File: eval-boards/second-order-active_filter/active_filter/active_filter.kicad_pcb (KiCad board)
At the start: 2 copper layers, 66 x 40 mm, 35 parts, among them J1 IN_A, J2 IN_B, J4 OUT_A, J5 OUT_B, U1 ADA4075-2

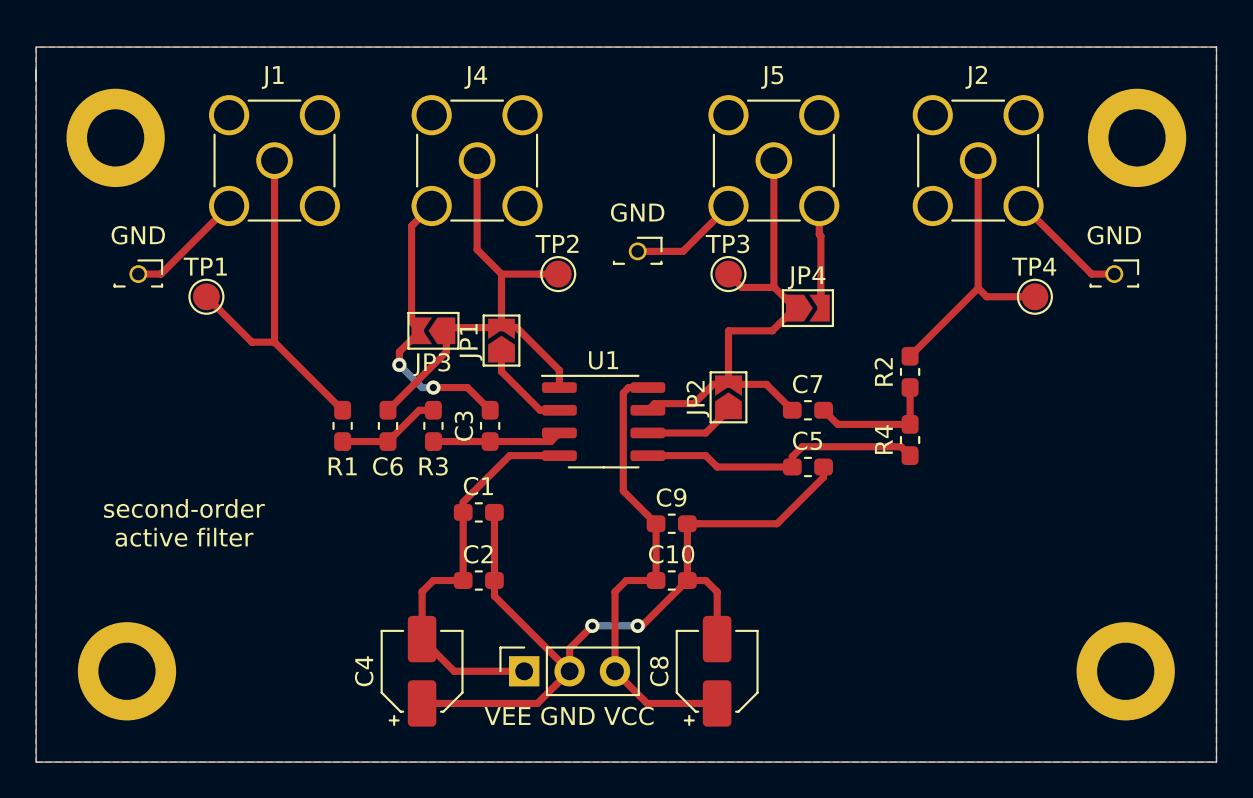
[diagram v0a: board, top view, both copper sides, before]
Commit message: power_and_RF_updated
修正了ADA4817和有源滤波器的电源线管脚、反馈电阻和焊盘handsold
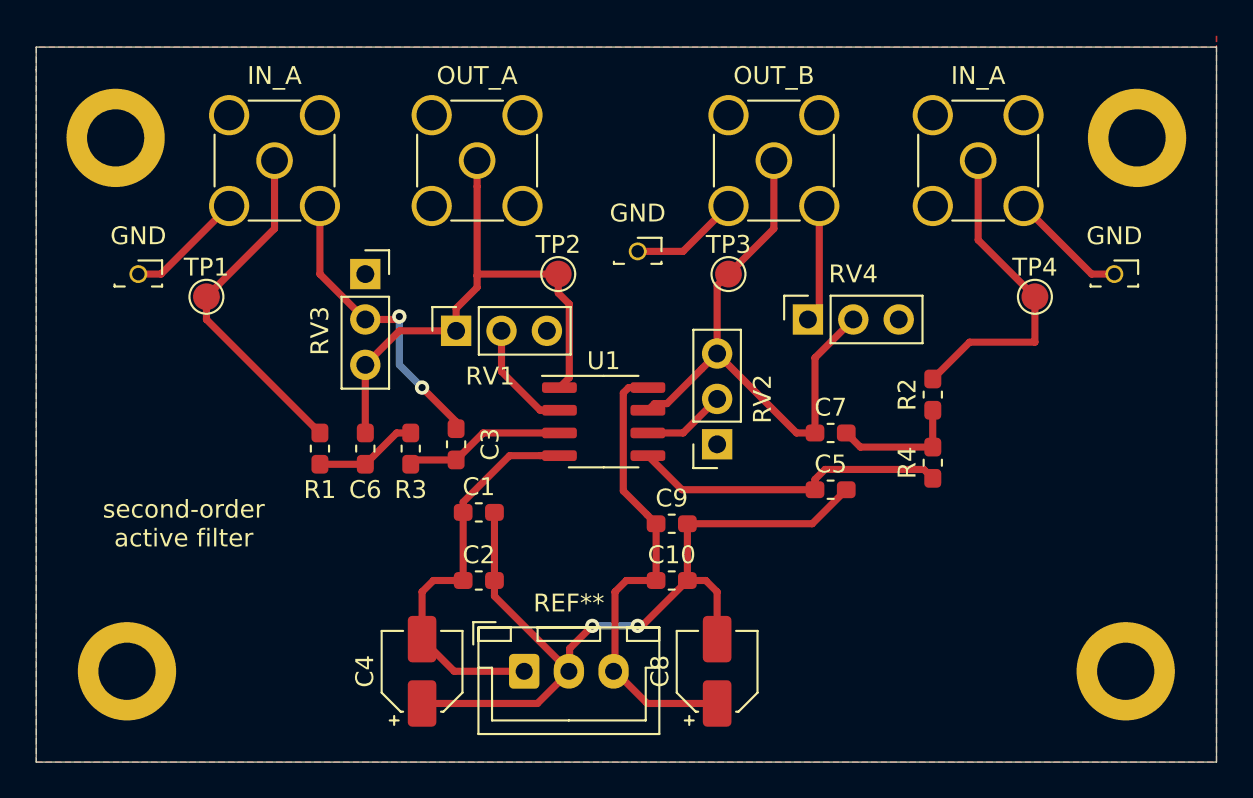
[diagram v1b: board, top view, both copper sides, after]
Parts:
- removed JP1, JP2, JP3, JP4: Jumper_2_Bridged, Jumper:SolderJumper-2_P1.3mm_Open_TrianglePad1.0x1.5mm
- removed VEE GND VCC: Conn_01x03_Male, Connector_PinSocket_2.54mm:PinSocket_1x03_P2.54mm_Vertical
- added REF**: JST_XH_B3B-XH-A_1x03_P2.50mm_Vertical, Connector_JST:JST_XH_B3B-XH-A_1x03_P2.50mm_Vertical, F.Cu at (137.2, 106.7)
- added RV1: PinSocket_1x03_P2.54mm_Vertical, Connector_PinSocket_2.54mm:PinSocket_1x03_P2.54mm_Vertical, F.Cu at (133.3, 87.6)
- added RV2: PinSocket_1x03_P2.54mm_Vertical, Connector_PinSocket_2.54mm:PinSocket_1x03_P2.54mm_Vertical, F.Cu at (148.0, 94.0)
- added RV3: PinSocket_1x03_P2.54mm_Vertical, Connector_PinSocket_2.54mm:PinSocket_1x03_P2.54mm_Vertical, F.Cu at (128.3, 84.5)
- added RV4: PinSocket_1x03_P2.54mm_Vertical, Connector_PinSocket_2.54mm:PinSocket_1x03_P2.54mm_Vertical, F.Cu at (153.0, 87.0)
- moved C3 2.17 mm to (133.3, 94.0)
- moved R4 1.80 mm to (160.0, 95.0)
- moved C5 1.80 mm to (154.3, 96.5)
- moved C7 1.80 mm to (154.3, 93.3)
- moved R2 1.80 mm to (160.0, 91.2)
- moved R3 1.80 mm to (130.8, 94.2)
- moved R1 1.80 mm to (125.7, 94.2)
- moved C6 1.80 mm to (128.3, 94.2)
- renumbered J1 to IN_A, J2 to IN_A, J4 to OUT_A, J5 to OUT_B
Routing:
- net Net-(C6-Pad1): track 27.2 -> 31.1 mm
- net Net-(C7-Pad1): track 28.1 -> 31.9 mm
- net Net-(J2-Pad1): track 15.9 -> 18.0 mm
- net GND: track 87.5 -> 89.5 mm
- net Net-(C5-Pad1): track 15.9 -> 17.7 mm
- net Net-(C3-Pad1): track 7.25 -> 9.04 mm
- net Net-(JP1-Pad1): track 5.15 -> 6.42 mm
- net Net-(J1-Pad1): track 20.4 -> 19.4 mm
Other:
- outline, holes or cut-outs redrawn
